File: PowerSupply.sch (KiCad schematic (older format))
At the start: 69 parts

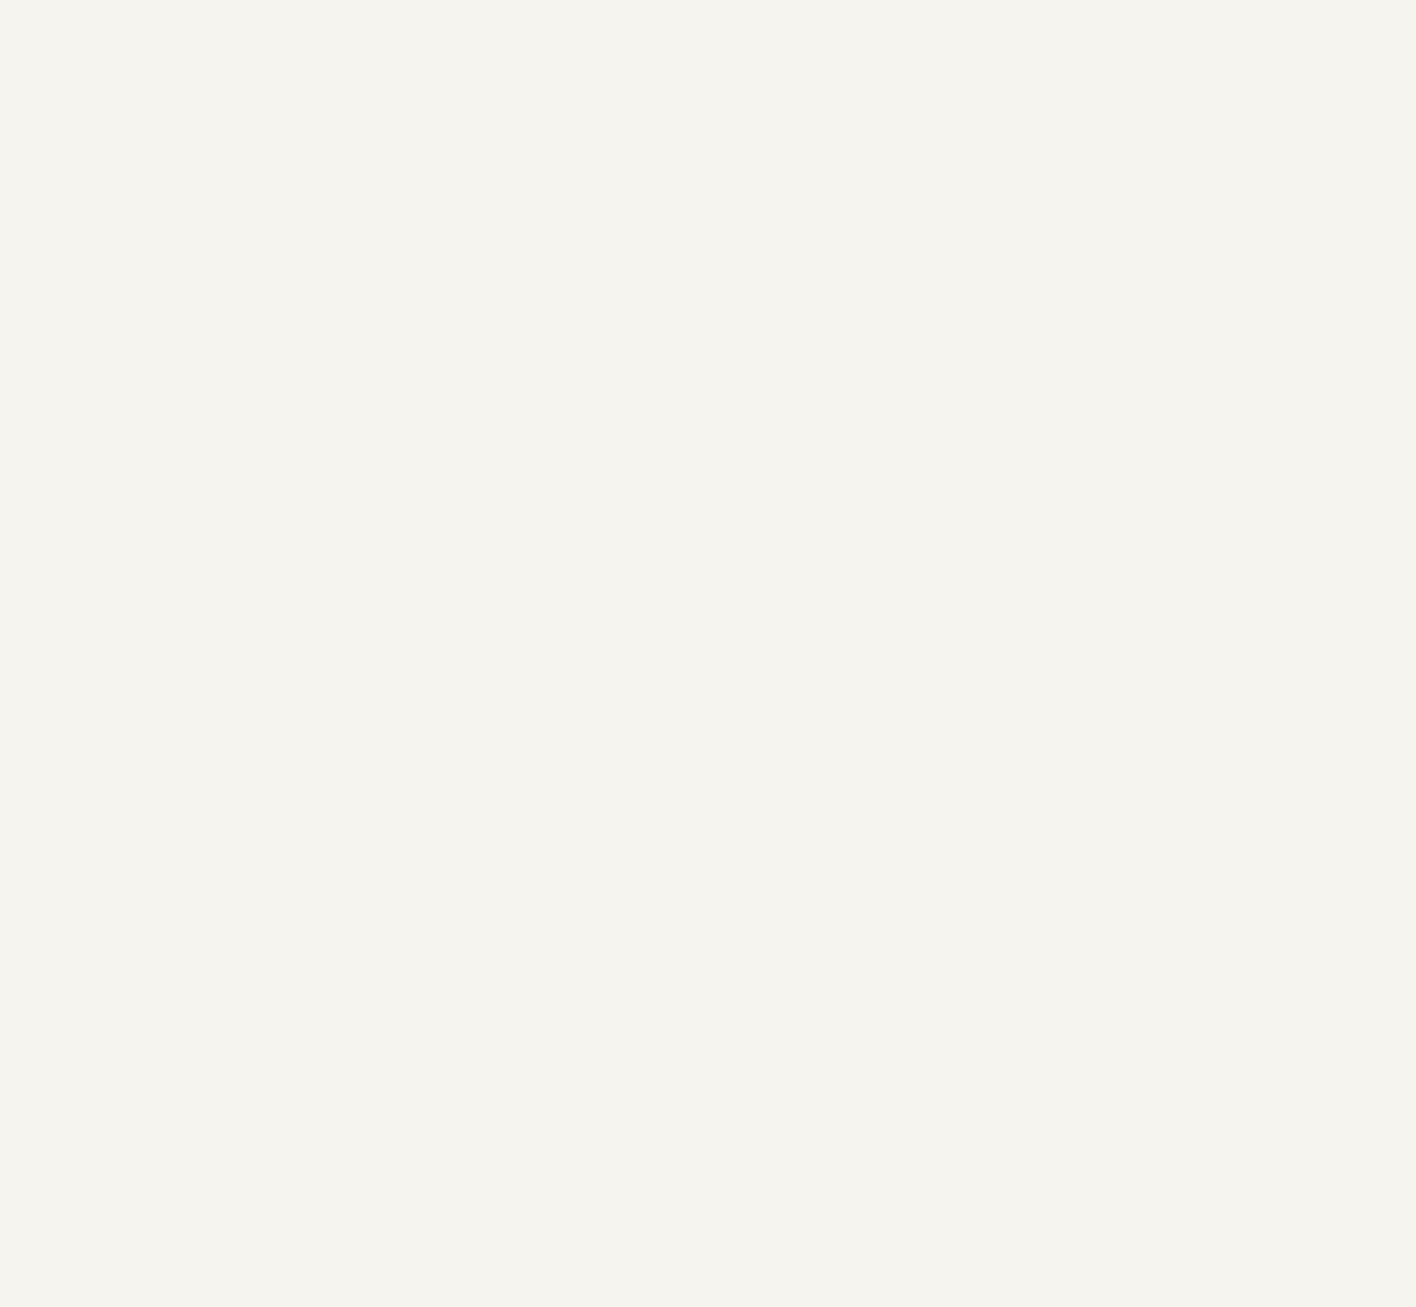
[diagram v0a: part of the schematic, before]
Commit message: [added:] 5V buck converter enable circuit [added:] RPi power up circuit
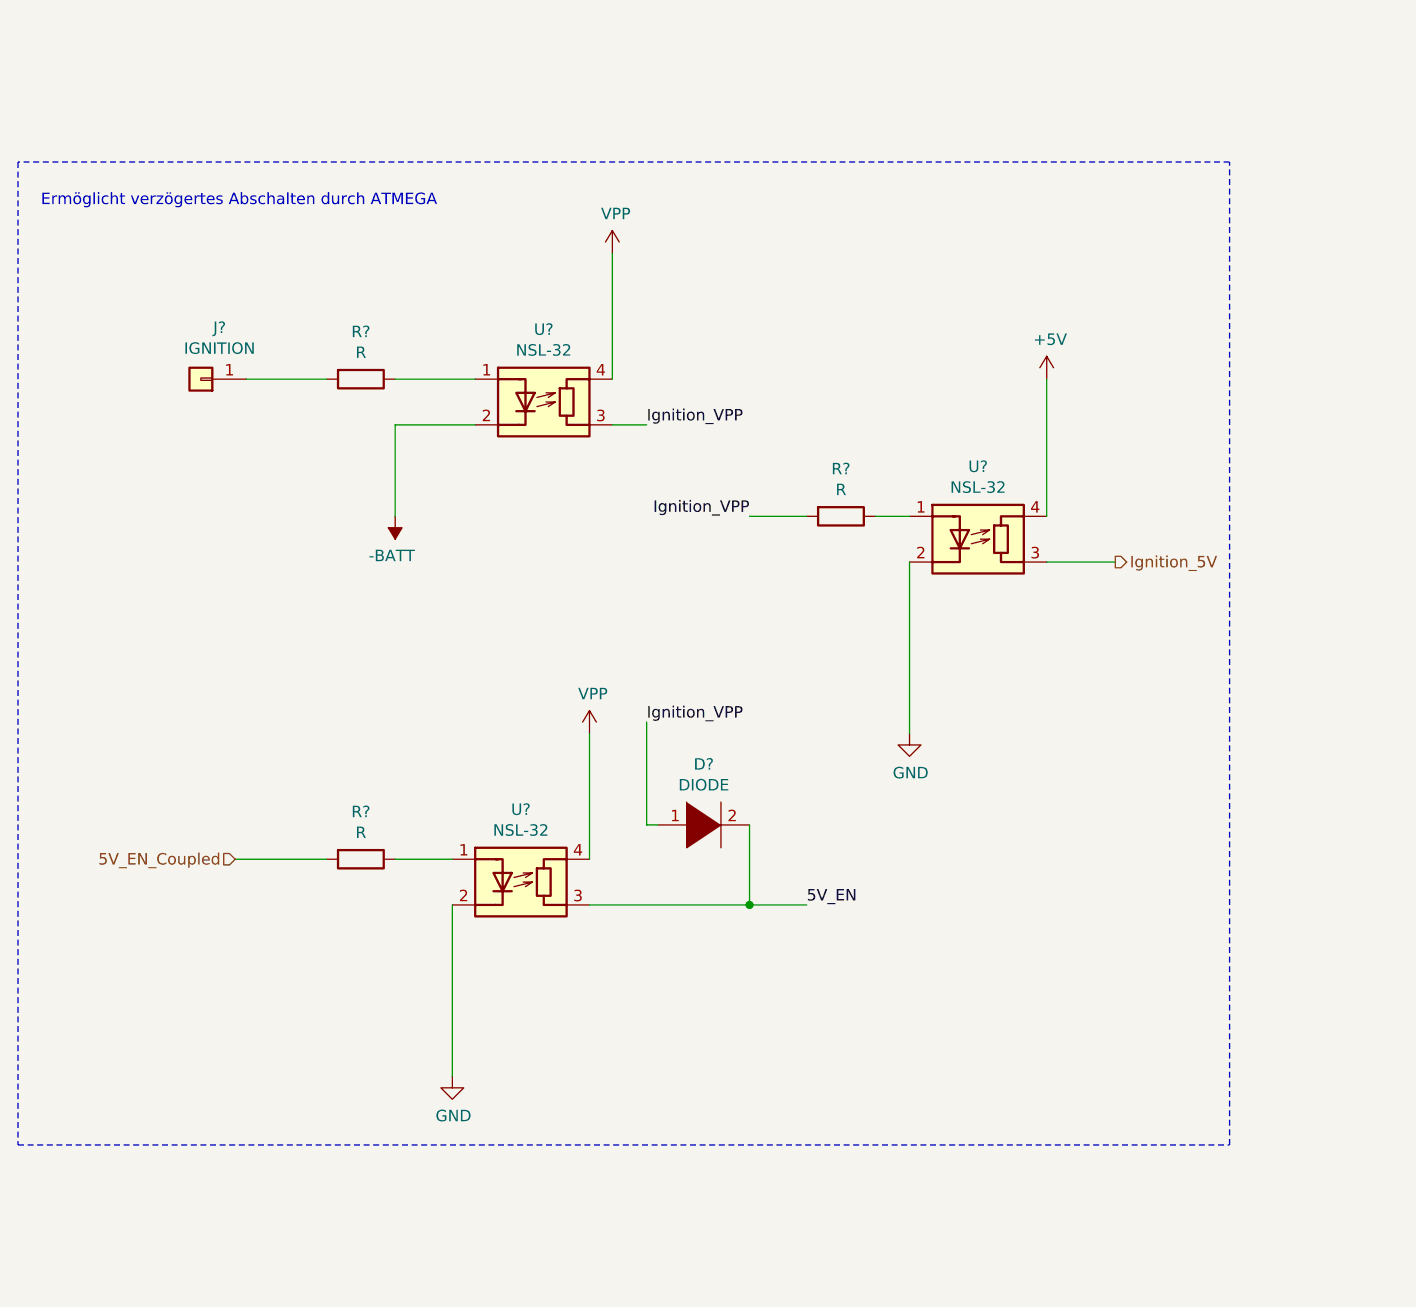
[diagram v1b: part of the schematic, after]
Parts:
- added D?: DIODE, symbol pspice:DIODE
- added J?: IGNITION, symbol Connector_Generic:Conn_01x01
- added R? (x3): R, symbol Device:R
- added U? (x3): NSL-32, OptoDevice:Luna_NSL-32, symbol Isolator:NSL-32
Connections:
- net +5V: now also U?.4 (R)
- net -BATT: now also U?.2 (K)
- net GND: now also U?.2 (K), U?.2 (K)
- net VPP: now also U?.4 (R), U?.4 (R)
- new net: R?.1, U?.1 (A) (x3)
- new net: J?.1 (Pin_1), R?.2
- new net 5V_EN: D?.2 (A), U?.3 (R)
- new net 5V_EN_Coupled: R?.2
- new net Ignition_5V: U?.3 (R)
- new net Ignition_VPP: D?.1 (K), R?.2, U?.3 (R)
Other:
- note added: "Ermöglicht verzögertes Abschalten durch ATMEGA"
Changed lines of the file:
@@
 Wire Wire Line
 	10900 2500 11300 2500
+$Comp
+L power:VPP #PWR?
+U 1 1 60D96107
+P -2400 8100
+F 0 "#PWR?" H -2400 7950 50  0001 C CNN
+F 1 "VPP" H -2385 8273 50  0000 C CNN
+F 2 "" H -2400 8100 50  0001 C CNN
+F 3 "" H -2400 8100 50  0001 C CNN
+	1    -2400 8100
+	1    0    0    -1
+$EndComp
+Text HLabel -4050 10750 0    50   Input ~ 0
+5V_EN_Coupled
+$Comp
+L power:GND #PWR?
+U 1 1 60DC4DCB
+P -1100 10200
+F 0 "#PWR?" H -1100 9950 50  0001 C CNN
+F 1 "GND" H -1095 10027 50  0000 C CNN
+F 2 "" H -1100 10200 50  0001 C CNN
+F 3 "" H -1100 10200 50  0001 C CNN
+	1    -1100 10200
+	1    0    0    -1
+$EndComp
+Text HLabel -200 9450 2    50   Output ~ 0
+Ignition_5V
+Text Label -1550 10950 0    50   ~ 0
+5V_EN
+$Comp
+L power:-BATT #PWR?
+U 1 1 60E53236
+P -3350 9250
+F 0 "#PWR?" H -3350 9100 50  0001 C CNN
+F 1 "-BATT" H -3335 9423 50  0000 C CNN
+F 2 "" H -3350 9250 50  0001 C CNN
+F 3 "" H -3350 9250 50  0001 C CNN
+	1    -3350 9250
+	-1   0    0    1
+$EndComp
+Wire Wire Line
+	-3350 9250 -3350 8850
+Wire Wire Line
+	-3350 8850 -3000 8850
+Wire Wire Line
+	-3000 8650 -3350 8650
+$Comp
+L Isolator:NSL-32 U?
+U 1 1 60EE3D3B
+P -800 9350
+F 0 "U?" H -800 9667 50  0000 C CNN
+F 1 "NSL-32" H -800 9576 50  0000 C CNN
+F 2 "OptoDevice:Luna_NSL-32" H -800 9050 50  0001 C CNN
+F 3 "http://lunainc.com/wp-content/uploads/2016/06/NSL-32.pdf" H -750 9350 50  0001 C CNN
+	1    -800 9350
+	1    0    0    -1
+$EndComp
+$Comp
+L power:+5V #PWR?
+U 1 1 60F76FDA
+P -500 8650
+F 0 "#PWR?" H -500 8500 50  0001 C CNN
+F 1 "+5V" H -485 8823 50  0000 C CNN
+F 2 "" H -500 8650 50  0001 C CNN
+F 3 "" H -500 8650 50  0001 C CNN
+	1    -500 8650
+	1    0    0    -1
+$EndComp
+Wire Wire Line
+	-1250 9250 -1100 9250
+Wire Wire Line
+	-2400 8850 -2250 8850
+$Comp
+L Isolator:NSL-32 U?
+U 1 1 60E503E3
+P -2700 8750
+F 0 "U?" H -2700 9067 50  0000 C CNN
+F 1 "NSL-32" H -2700 8976 50  0000 C CNN
+F 2 "OptoDevice:Luna_NSL-32" H -2700 8450 50  0001 C CNN
+F 3 "http://lunainc.com/wp-content/uploads/2016/06/NSL-32.pdf" H -2650 8750 50  0001 C CNN
+	1    -2700 8750
+	1    0    0    -1
+$EndComp
+Wire Wire Line
+	-2400 8650 -2400 8100
+Wire Wire Line
+	-1100 9450 -1100 10200
+Wire Wire Line
+	-500 9250 -500 8650
+Wire Wire Line
+	-500 9450 -200 9450
+$Comp
+L Isolator:NSL-32 U?
+U 1 1 61106169
+P -2800 10850
+F 0 "U?" H -2800 11167 50  0000 C CNN
+F 1 "NSL-32" H -2800 11076 50  0000 C CNN
+F 2 "OptoDevice:Luna_NSL-32" H -2800 10550 50  0001 C CNN
+F 3 "http://lunainc.com/wp-content/uploads/2016/06/NSL-32.pdf" H -2750 10850 50  0001 C CNN
+	1    -2800 10850
+	1    0    0    -1
+$EndComp
+Wire Wire Line
+	-3350 10750 -3100 10750
+$Comp
+L power:GND #PWR?
+U 1 1 6119BF29
+P -3100 11700
+F 0 "#PWR?" H -3100 11450 50  0001 C CNN
+F 1 "GND" H -3095 11527 50  0000 C CNN
+F 2 "" H -3100 11700 50  0001 C CNN
+F 3 "" H -3100 11700 50  0001 C CNN
+	1    -3100 11700
+	1    0    0    -1
+$EndComp
+Wire Wire Line
+	-3100 10950 -3100 11700
+$Comp
+L power:VPP #PWR?
+U 1 1 611CEBBE
+P -2500 10200
+F 0 "#PWR?" H -2500 10050 50  0001 C CNN
+F 1 "VPP" H -2485 10373 50  0000 C CNN
+F 2 "" H -2500 10200 50  0001 C CNN
+F 3 "" H -2500 10200 50  0001 C CNN
+	1    -2500 10200
+	1    0    0    -1
+$EndComp
+Wire Wire Line
+	-2500 10750 -2500 10200
+Text Label -2250 8850 0    50   ~ 0
+Ignition_VPP
+Text Label -1800 9250 2    50   ~ 0
+Ignition_VPP
+$Comp
+L pspice:DIODE D?
+U 1 1 612EFD78
+P -2000 10600
+F 0 "D?" H -2000 10865 50  0000 C CNN
+F 1 "DIODE" H -2000 10774 50  0000 C CNN
+F 2 "" H -2000 10600 50  0001 C CNN
+F 3 "~" H -2000 10600 50  0001 C CNN
+	1    -2000 10600
+	1    0    0    -1
+$EndComp
+Wire Wire Line
+	-1800 10600 -1800 10950
+Wire Wire Line
+	-1800 10950 -1550 10950
+Wire Wire Line
+	-2500 10950 -1800 10950
+Connection ~ -1800 10950
+Text Label -2250 10150 0    50   ~ 0
+Ignition_VPP
+Wire Wire Line
+	-2250 10150 -2250 10600
+Wire Wire Line
+	-2250 10600 -2200 10600
+$Comp
+L Device:R R?
+U 1 1 613760CF
+P -3500 8650
+F 0 "R?" V -3707 8650 50  0000 C CNN
+F 1 "R" V -3616 8650 50  0000 C CNN
+F 2 "" V -3570 8650 50  0001 C CNN
+F 3 "~" H -3500 8650 50  0001 C CNN
+	1    -3500 8650
+	0    1    1    0
+$EndComp
+$Comp
+L Device:R R?
+U 1 1 613FB201
+P -3500 10750
+F 0 "R?" V -3707 10750 50  0000 C CNN
+F 1 "R" V -3616 10750 50  0000 C CNN
+F 2 "" V -3570 10750 50  0001 C CNN
+F 3 "~" H -3500 10750 50  0001 C CNN
+	1    -3500 10750
+	0    1    1    0
+$EndComp
+Wire Wire Line
+	-3650 10750 -4050 10750
+$Comp
+L Device:R R?
+U 1 1 6146556A
+P -1400 9250
+F 0 "R?" V -1607 9250 50  0000 C CNN
+F 1 "R" V -1516 9250 50  0000 C CNN
+F 2 "" V -1470 9250 50  0001 C CNN
+F 3 "~" H -1400 9250 50  0001 C CNN
+	1    -1400 9250
+	0    1    1    0
+$EndComp
+Wire Wire Line
+	-1800 9250 -1550 9250
+Wire Notes Line
+	-5000 12000 300  12000
+Wire Notes Line
+	300  12000 300  7700
+Wire Notes Line
+	300  7700 -5000 7700
+Wire Notes Line
+	-5000 7700 -5000 12000
+Text Notes -4900 7900 0    50   ~ 0
+Ermöglicht verzögertes Abschalten durch ATMEGA
+$Comp
+L Connector_Generic:Conn_01x01 J?
+U 1 1 6150EB49
+P -4200 8650
+F 0 "J?" H -4282 8425 50  0000 C CNN
+F 1 "IGNITION" H -4282 8516 50  0000 C CNN
+F 2 "" H -4200 8650 50  0001 C CNN
+F 3 "~" H -4200 8650 50  0001 C CNN
+	1    -4200 8650
+	-1   0    0    1
+$EndComp
+Wire Wire Line
+	-3650 8650 -4000 8650
 $EndSCHEMATC

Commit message: - BT fertig, warten auf Rueckmeldung von Microchip - CM3 fast fertig - diverse Kleinigkeiten
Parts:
- removed J?: IGNITION, symbol Connector_Generic:Conn_01x01
- added J11: IGNITION, Connector_PinHeader_2.54mm:PinHeader_1x02_P2.54mm_Horizontal, symbol Connector_Generic:Conn_01x02
- gave numbers to parts that had none: 76
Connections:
- net -BATT: now also J11.2 (Pin_2)
- net at R19.2: now also J11.1 (Pin_1)
